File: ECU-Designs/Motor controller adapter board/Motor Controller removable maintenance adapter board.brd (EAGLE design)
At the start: 33.2 x 36.4 mm, 5 parts, among them X1 MINIFIT_5566-6

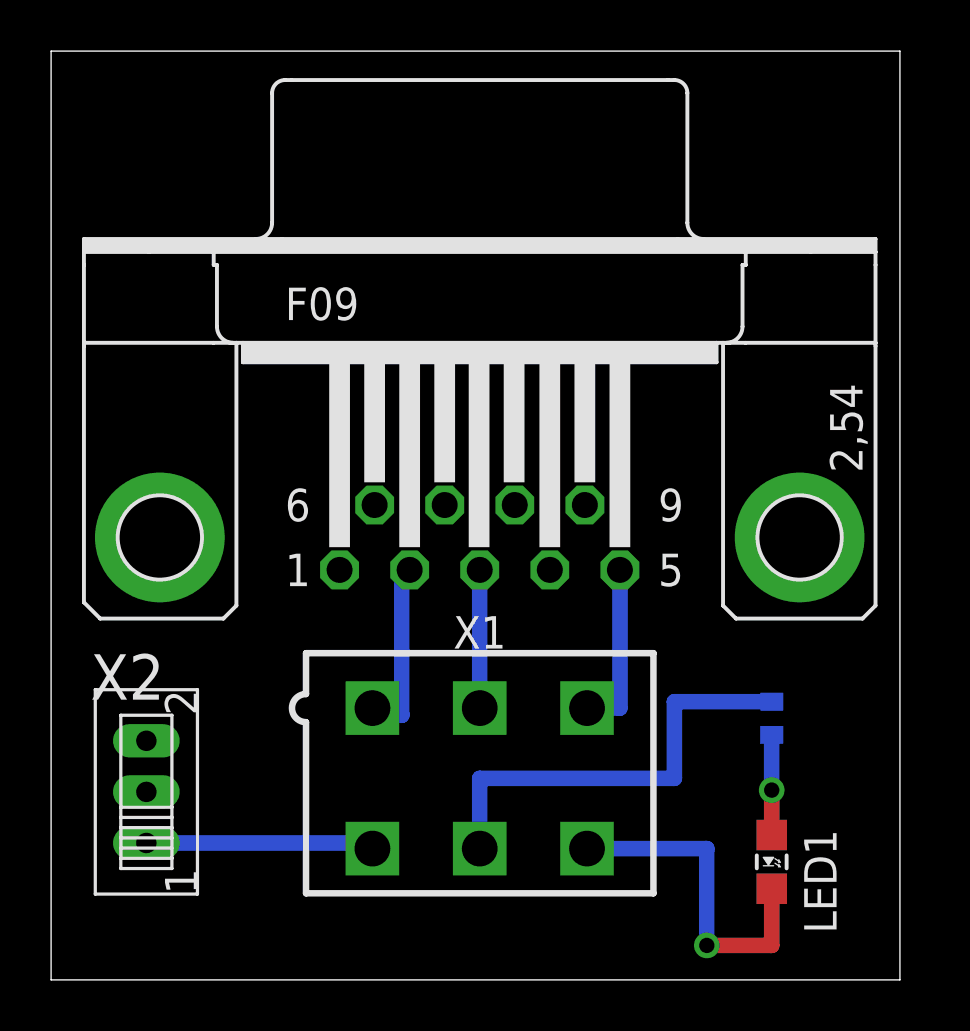
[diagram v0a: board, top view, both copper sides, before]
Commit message: Updated moter controller board with switch designation
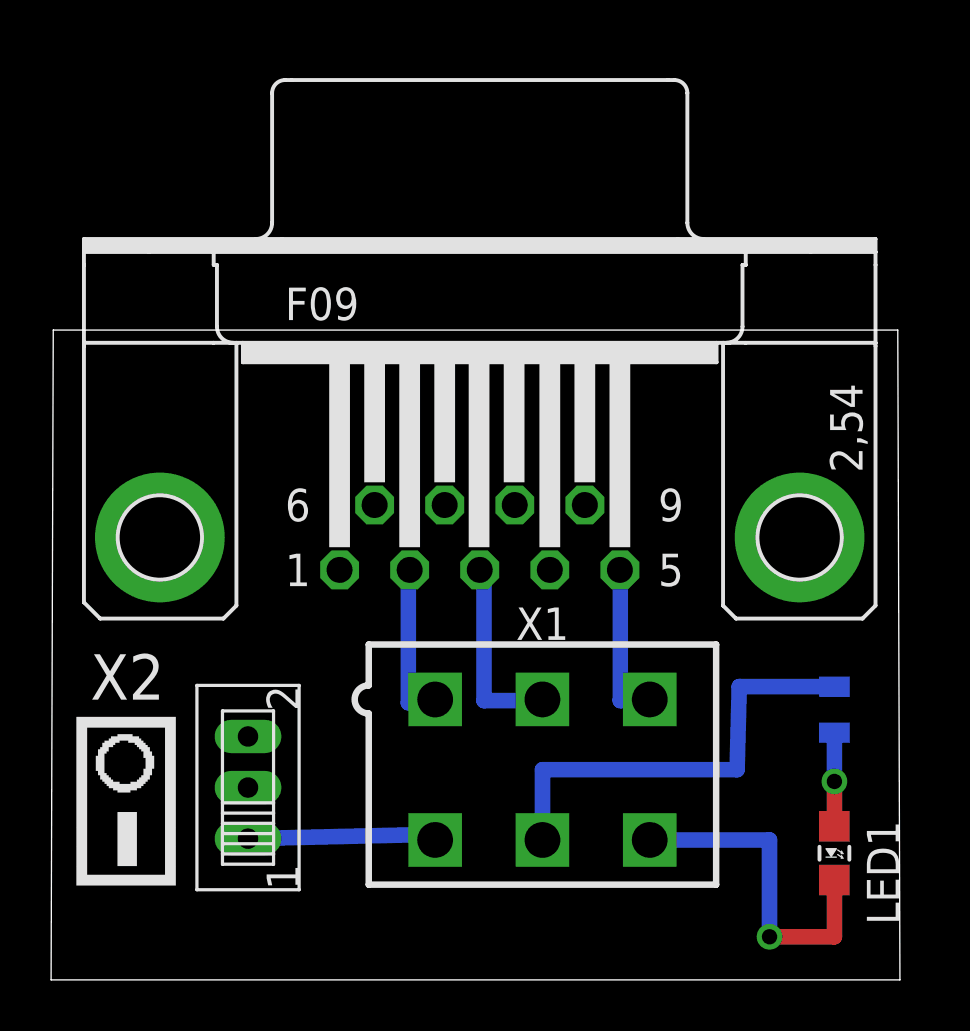
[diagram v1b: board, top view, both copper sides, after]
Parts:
- R1: device HyTechDevices:0402-RES -> HyTechDevices:0805
- moved U$1 3.98 mm to (9.98, 49.2)
- moved LED1 2.48 mm to (32.9, 46.6)
- moved R1 2.48 mm to (32.9, 52.2)
- moved X1 2.48 mm to (21.5, 49.9)
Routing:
- net N$7: track 5.41 -> 7.62 mm
- net N$4: track 9.07 -> 7.55 mm
- net N$6: track 7.43 -> 6.44 mm
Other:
- board size 33.2 x 36.4 mm -> 33.2 x 25.4 mm
